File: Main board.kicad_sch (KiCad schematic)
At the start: 103 parts, among them CN1 PA001-6P, CN2 PA001-6P, J1 Conn_ARM_SWD_TagConnect_TC203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, J2 Conn_01x02_Pin, J3 Conn_01x02_Pin, J5 Connector, USB-TYPE-C-16P, J6 436500201, J7 Conn_01x02_Pin, J8 Conn_01x04_Pin, Q1 SI7232DN-T1-GE3, Q2 SI7232DN-T1-GE3, SW1 SKRKAEE020, SW2 SKRKAEE020, SW3 SW_SPDT, SW4 SW_SPDT, U1 STM32U575VGTx, U10 TLV75733PDBV, U11 NRVB120VLSFT1G, U12 NRVB120VLSFT1G, U2 TPS62901RPJR, U7 SN74AHCT125DR, X1 1XXD32000MBA, Y1 ECS-327TXO-33-TR

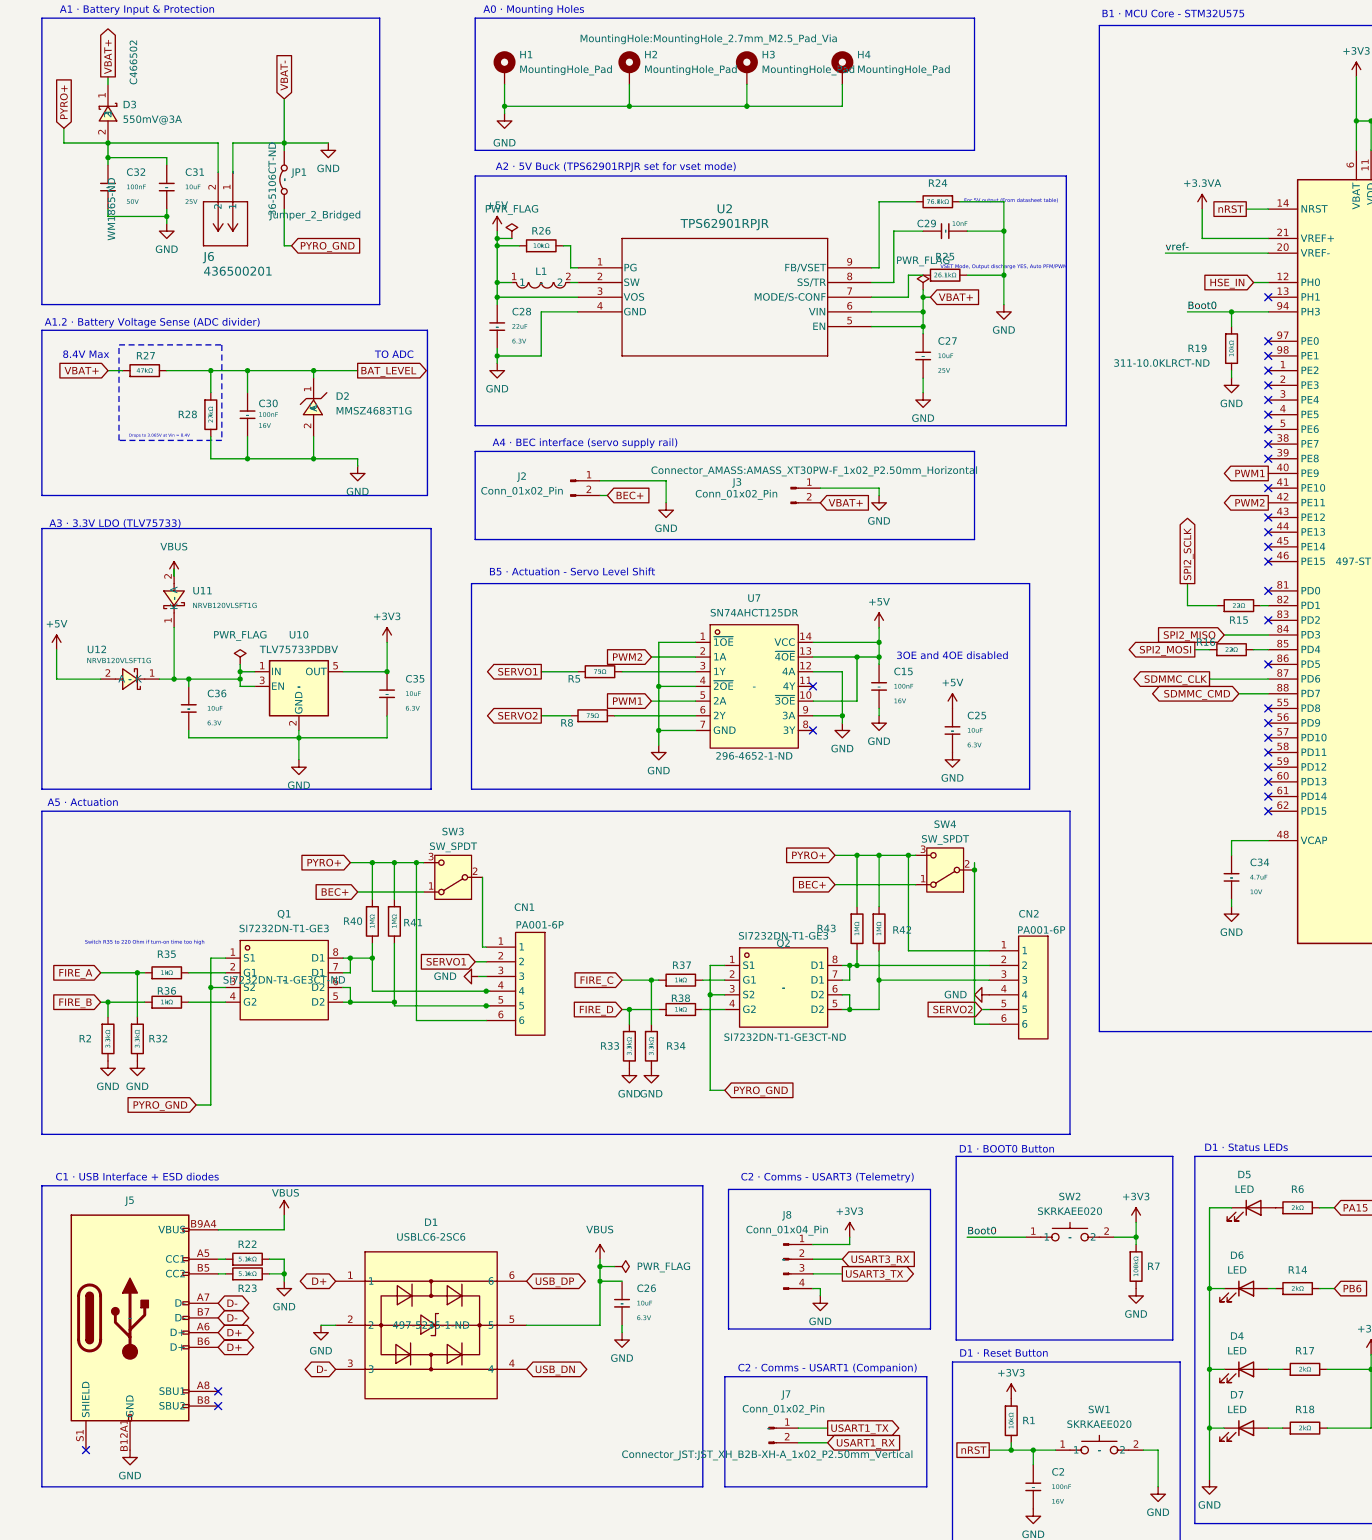
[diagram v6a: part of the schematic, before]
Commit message: Change switch footprint to C&K 1101M2S3CQE2
For handling PYRO power and temp
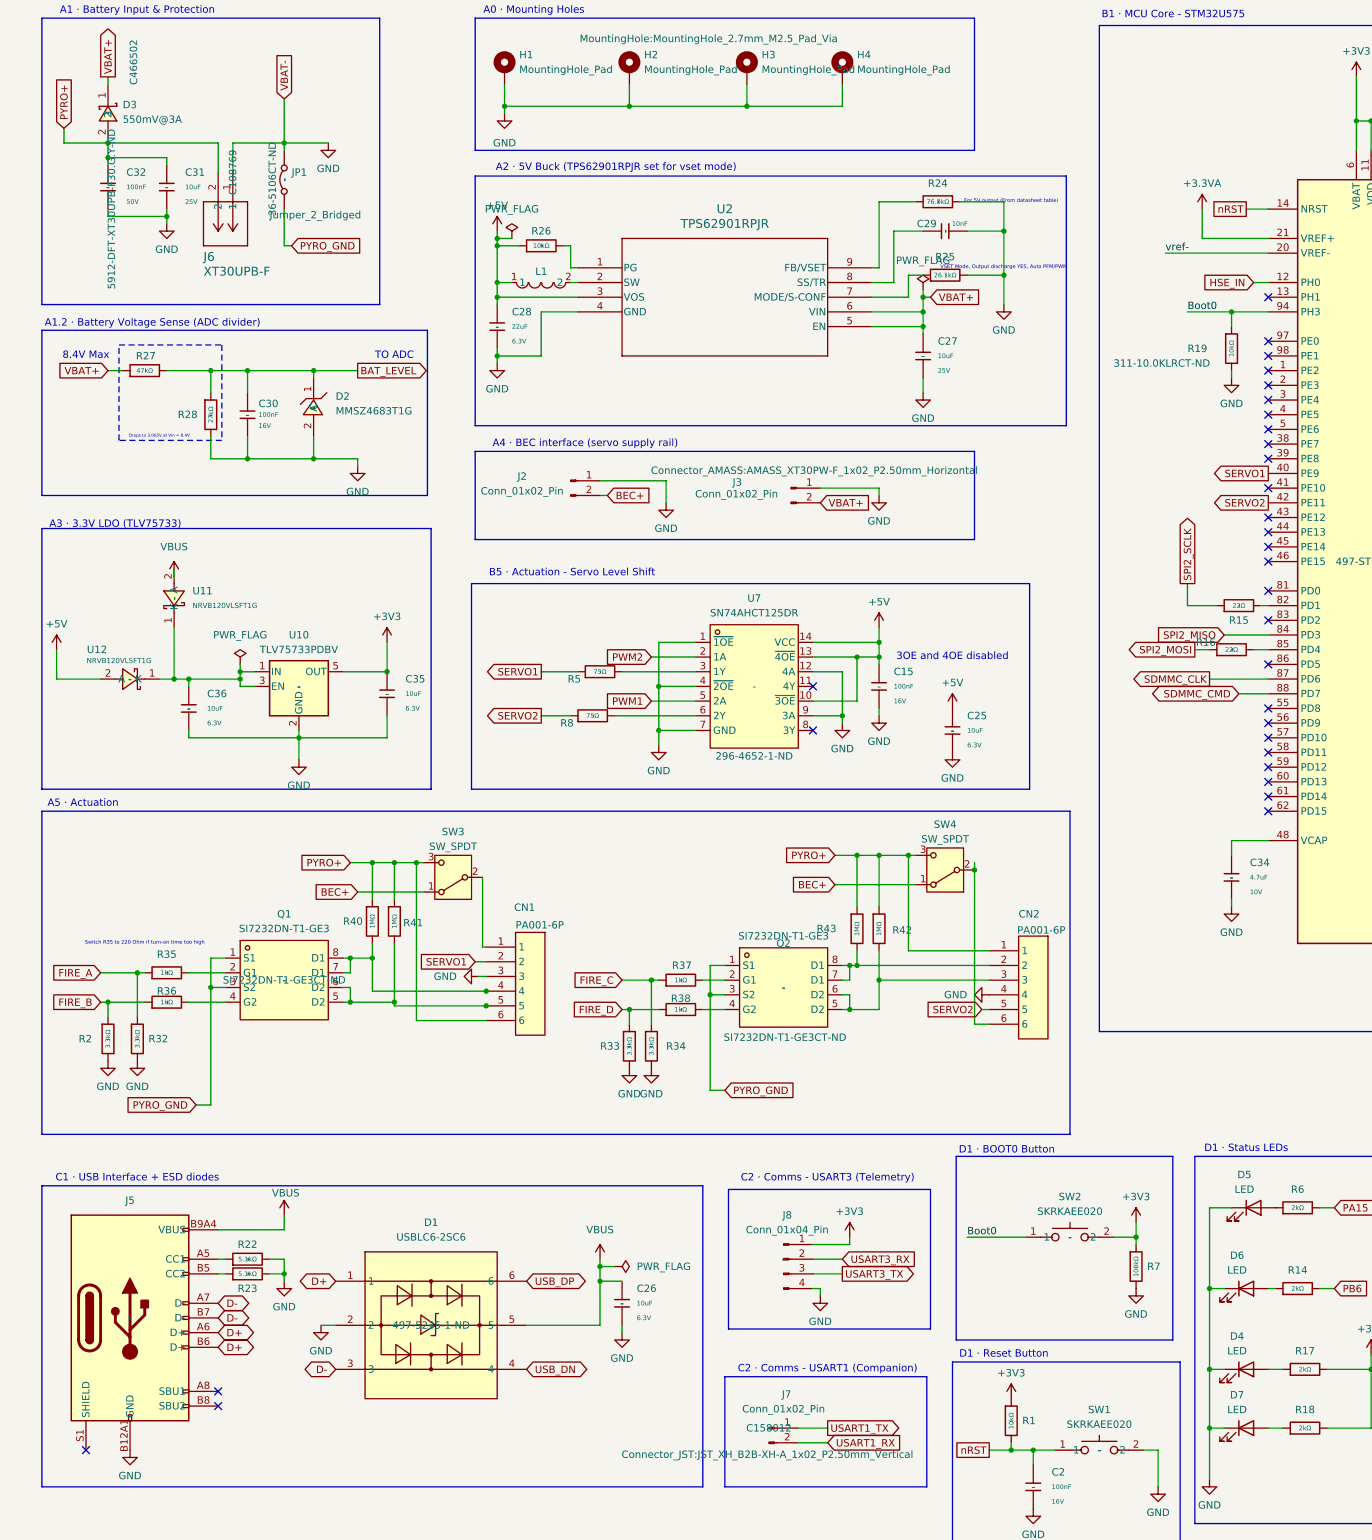
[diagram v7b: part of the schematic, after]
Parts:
- C15, C25, R5, R8, U7: now left out of the parts list
- J6: value 436500201 -> XT30UPB-F; Digikey Part No. WM1865-ND -> 5912-DFT-XT30UPB-F30.G.Y-ND; LCSC - -> C108769
- J7: Digikey Part No. WM10667-ND -> 455-B2B-XH-A-ND; LCSC - -> C158012
- L1: LCSC C354573 -> C354578
- R24: Class Preferred Component -> (none); LCSC C22764 -> C165743; Manufacturer UNI-ROYAL(Uniroyal Elec) -> YAGEO; Part 0603WAF1101T5E -> RC0603FR-0776K8L; Price 0.004USD -> (none); Resistance 1.1kΩ -> 76.8kΩ; Stock 156127 -> (none)
- R25: Class Preferred Component -> (none); LCSC C22764 -> C482816; Manufacturer UNI-ROYAL(Uniroyal Elec) -> YAGEO; Part 0603WAF1101T5E -> RC0603FR-0726K1L; Price 0.004USD -> (none); Resistance 1.1kΩ -> 26.1kΩ; Stock 156127 -> (none)
- SW3, SW4: footprint EasyEDA:SW-TH_3P-L8.8-W3.9-P2.50_SS12D00G3 -> Mainboard_local:SW-TH_1101M2S3CQE2
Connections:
- net PWM1: no longer U1.40 (PE9)
- net PWM2: no longer U1.42 (PE11)
- net SERVO1: now also U1.40 (PE9)
- net SERVO2: now also U1.42 (PE11)
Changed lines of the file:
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@@
 		)
 	)
-	(global_label "PWM2"
+	(global_label "SERVO2"
 		(shape output)
 		(at 227.33 99.06 180)
@@
 		)
 		(property "Intersheetrefs" "${INTERSHEET_REFS}"
-			(at 218.9625 99.06 0)
+			(at 217.0877 99.06 0)
 			(effects
 				(font
@@
 		)
 	)
-	(global_label "PWM1"
+	(global_label "SERVO1"
 		(shape output)
 		(at 227.33 93.98 180)
@@
 		)
 		(property "Intersheetrefs" "${INTERSHEET_REFS}"
-			(at 218.9625 93.98 0)
+			(at 217.0877 93.98 0)
 			(effects
 				(font
@@
 			)
 		)
-		(property "Footprint" "EasyEDA:SW-TH_3P-L8.8-W3.9-P2.50_SS12D00G3"
+		(property "Footprint" "Mainboard_local:SW-TH_1101M2S3CQE2"
 			(at 171.45 162.56 0)
 			(effects
@@
 			)
 		)
-		(property "Footprint" "EasyEDA:SW-TH_3P-L8.8-W3.9-P2.50_SS12D00G3"
+		(property "Footprint" "Mainboard_local:SW-TH_1101M2S3CQE2"
 			(at 86.36 163.83 0)
 			(effects
@@
 		(mirror y)
 		(unit 1)
-		(exclude_from_sim no)
-		(in_bom yes)
-		(on_board yes)
+		(exclude_from_sim yes)
+		(in_bom no)
+		(on_board no)
 		(dnp no)
 		(property "Reference" "#PWR84"
@@
 		(mirror y)
 		(unit 1)
-		(exclude_from_sim no)
-		(in_bom yes)
-		(on_board yes)
+		(exclude_from_sim yes)
+		(in_bom no)
+		(on_board no)
 		(dnp no)
 		(property "Reference" "#PWR82"
@@
 			)
 		)
-		(property "Value" "436500201"
+		(property "Value" "XT30UPB-F"
 			(at 43.18 59.055 90)
 			(effects
@@
 			)
 		)
-		(property "Datasheet" "https://www.molex.com/en-us/products/part-detail-pdf/436500201?display=pdf"
+		(property "Datasheet" "https://www.lcsc.com/product-detail/C108769.html"
 			(at 48.26 41.91 0)
 			(effects
@@
 			)
 		)
-		(property "Digikey Part No." "WM1865-ND"
+		(property "Digikey Part No." "5912-DFT-XT30UPB-F30.G.Y-ND"
 			(at 27.305 48.26 0)
 			(effects
@@
 			)
 		)
-		(property "LCSC" "-"
+		(property "LCSC" "C108769"
 			(at 48.26 41.91 0)
 			(effects
@@
 		(at 160.02 120.65 0)
 		(unit 1)
-		(exclude_from_sim no)
-		(in_bom yes)
-		(on_board yes)
+		(exclude_from_sim yes)
+		(in_bom no)
+		(on_board no)
 		(dnp no)
 		(fields_autoplaced yes)
@@
 			)
 		)
-		(property "LCSC" "C354573"
+		(property "LCSC" "C354578"
 			(at 108.585 73.66 0)
 			(effects
@@
 		(at 160.02 130.81 0)
 		(unit 1)
-		(exclude_from_sim no)
-		(in_bom yes)
-		(on_board yes)
+		(exclude_from_sim yes)
+		(in_bom no)
+		(on_board no)
 		(dnp no)
 		(fields_autoplaced yes)
@@
 		(mirror y)
 		(unit 1)
-		(exclude_from_sim no)
-		(in_bom yes)
-		(on_board yes)
+		(exclude_from_sim yes)
+		(in_bom no)
+		(on_board no)
 		(dnp no)
 		(property "Reference" "#PWR83"
@@
 			)
 		)
-		(property "LCSC" "C22764"
+		(property "LCSC" "C482816"
 			(at 171.45 59.69 0)
 			(effects
@@
 			)
 		)
-		(property "Stock" "156127"
+		(property "Stock" ""
 			(at 171.45 59.69 0)
 			(effects
@@
 			)
 		)
-		(property "Price" "0.004USD"
+		(property "Price" ""
 			(at 171.45 59.69 0)
 			(effects
@@
 			)
 		)
-		(property "Class" "Preferred Component"
+		(property "Class" ""
 			(at 171.45 59.69 0)
 			(effects
@@
 			)
 		)
-		(property "Manufacturer" "UNI-ROYAL(Uniroyal Elec)"
+		(property "Manufacturer" "YAGEO"
 			(at 171.45 59.69 0)
 			(effects
@@
 			)
 		)
-		(property "Part" "0603WAF1101T5E"
+		(property "Part" "RC0603FR-0726K1L"
 			(at 171.45 57.785 90)
 			(effects
@@
 			)
 		)
-		(property "Resistance" "1.1kΩ"
+		(property "Resistance" "26.1kΩ"
 			(at 171.45 59.69 0)
 			(effects
@@
 		(at 111.76 128.27 90)
 		(unit 1)
-		(exclude_from_sim no)
-		(in_bom yes)
-		(on_board yes)
+		(exclude_from_sim yes)
+		(in_bom no)
+		(on_board no)
 		(dnp no)
 		(property "Reference" "R5"
@@
 			)
 		)
-		(property "Digikey Part No." "WM10667-ND"
+		(property "Digikey Part No." "455-B2B-XH-A-ND"
 			(at 137.16 266.446 0)
 			(effects
@@
 			)
 		)
-		(property "LCSC" "-"
+		(property "LCSC" "C158012"
 			(at 140.97 259.08 0)
 			(effects
@@
 		(at 110.49 135.89 90)
 		(unit 1)
-		(exclude_from_sim no)
-		(in_bom yes)
-		(on_board yes)
+		(exclude_from_sim yes)
+		(in_bom no)
+		(on_board no)
 		(dnp no)
 		(property "Reference" "R8"
@@
 			)
 		)
-		(property "LCSC" "C22764"
+		(property "LCSC" "C165743"
 			(at 170.18 46.99 0)
 			(effects
@@
 			)
 		)
-		(property "Stock" "156127"
+		(property "Stock" ""
 			(at 170.18 46.99 0)
 			(effects
@@
 			)
 		)
-		(property "Price" "0.004USD"
+		(property "Price" ""
 			(at 170.18 46.99 0)
 			(effects
@@
 			)
 		)
-		(property "Class" "Preferred Component"
+		(property "Class" ""
 			(at 170.18 46.99 0)
 			(effects
@@
 			)
 		)
-		(property "Manufacturer" "UNI-ROYAL(Uniroyal Elec)"
+		(property "Manufacturer" "YAGEO"
 			(at 170.18 46.99 0)
 			(effects
@@
 			)
 		)
-		(property "Part" "0603WAF1101T5E"
+		(property "Part" "RC0603FR-0776K8L"
 			(at 170.18 45.085 90)
 			(effects
@@
 			)
 		)
-		(property "Resistance" "1.1kΩ"
+		(property "Resistance" "76.8kΩ"
 			(at 170.18 46.99 0)
 			(effects
@@
 		(at 172.72 138.43 0)
 		(unit 1)
-		(exclude_from_sim no)
-		(in_bom yes)
-		(on_board yes)
+		(exclude_from_sim yes)
+		(in_bom no)
+		(on_board no)
 		(dnp no)
 		(property "Reference" "C25"
@@
 		(mirror y)
 		(unit 1)
-		(exclude_from_sim no)
-		(in_bom yes)
-		(on_board yes)
+		(exclude_from_sim yes)
+		(in_bom no)
+		(on_board no)
 		(dnp no)
 		(property "Reference" "#PWR86"
@@
 		(at 172.72 134.62 0)
 		(unit 1)
-		(exclude_from_sim no)
-		(in_bom yes)
-		(on_board yes)
+		(exclude_from_sim yes)
+		(in_bom no)
+		(on_board no)
 		(dnp no)
 		(fields_autoplaced yes)
@@
 		(at 138.43 130.81 0)
 		(unit 1)
-		(exclude_from_sim no)
-		(in_bom yes)
-		(on_board yes)
+		(exclude_from_sim yes)
+		(in_bom no)
+		(on_board no)
 		(dnp no)
 		(property "Reference" "U7"

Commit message: New layout New.ioc
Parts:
- CN1, CN2: value PA001-6P -> KF127S-3.5-6P; footprint Mainboard_local:CONN-TH_6P-P5.00_PA001-6P -> TerminalBlock_Phoenix:TerminalBlock_Phoenix_PT-1,5-6-3.5-H_1x06_P3.50mm_Horizontal; LCSC Part C173288 -> C2974907; MPN PA001-6P -> KF127S-3.5-6P; Manufacturer 惠华 -> Cixi Kefa Elec
- H1, H2, H3, H4: footprint MountingHole:MountingHole_2.7mm_M2.5_Pad_Via -> MountingHole:MountingHole_2.2mm_M2_Pad_Via
- J3: value Conn_01x02_Pin -> Micro-Fit 43650-0215; footprint Connector_AMASS:AMASS_XT30PW-F_1x02_P2.50mm_Horizontal -> Connector_Molex:Molex_Micro-Fit_3.0_43650-0215_1x02_P3.00mm_Vertical; LCSC Part (none) -> C293740; MPN (none) -> 43650-0215
- J6: value XT30UPB-F -> Micro-Fit 43650-0215; footprint Connector_AMASS:AMASS_XT30UPB-F_1x02_P5.0mm_Vertical -> Connector_Molex:Molex_Micro-Fit_3.0_43650-0215_1x02_P3.00mm_Vertical; LCSC C108769 -> C293740; MANUFACTURER (none) -> Molex; MPN (none) -> 43650-0215
- JP3: renamed from SW3; value SW_SPDT -> BEC 1-2 / PYRO 2-3; footprint Mainboard_local:SW-TH_1101M2S3CQE2 -> Jumper:SolderJumper-3_P1.3mm_Open_Pad1.0x1.5mm_NumberLabels; symbol Switch:SW_SPDT -> Jumper:SolderJumper_3_Open; now left out of the parts list
- JP4: renamed from SW4; value SW_SPDT -> BEC 1-2 / PYRO 2-3; footprint Mainboard_local:SW-TH_1101M2S3CQE2 -> Jumper:SolderJumper-3_P1.3mm_Open_Pad1.0x1.5mm_NumberLabels; symbol Switch:SW_SPDT -> Jumper:SolderJumper_3_Open; now left out of the parts list
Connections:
- net FIRE_A: now also R2.1, R36.1; no longer R32.1, R35.1
- net FIRE_B: now also R32.1, R35.1; no longer R2.1, R36.1
- net SERVO1: now also CN1.4; no longer CN1.2
- net SERVO2: now also CN2.3; no longer CN2.5
- net at JP4.2 (C): now also CN2.2; no longer CN2.6
- net at JP3.2 (C): now also CN1.5; no longer CN1.1
- net at Q1.5 (D2), Q1.6 (D2), R41.2: now also CN1.1; no longer CN1.5
- net at Q1.7 (D1), Q1.8 (D1), R40.2: now also CN1.2; no longer CN1.4
- net at Q2.5 (D2), Q2.6 (D2), R42.2: now also CN2.5; no longer CN2.3
- net at Q2.7 (D1), Q2.8 (D1), R43.2: now also CN2.6; no longer CN2.2
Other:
- moved on the sheet: CN1, R40
